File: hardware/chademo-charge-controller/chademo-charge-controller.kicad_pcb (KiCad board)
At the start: 2 copper layers, 136 x 120 mm, 26 parts, among them IC1 TPS62160DGKR, IC2 MCP2515-I_ST, IC3 SN65HVD230, IC4 MCP2515-I_ST, IC5 SN65HVD230, IC6 NCV8402ASTT1G, J1 M22-2510346, U1 Pico, U2 PC817, U3 PC817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

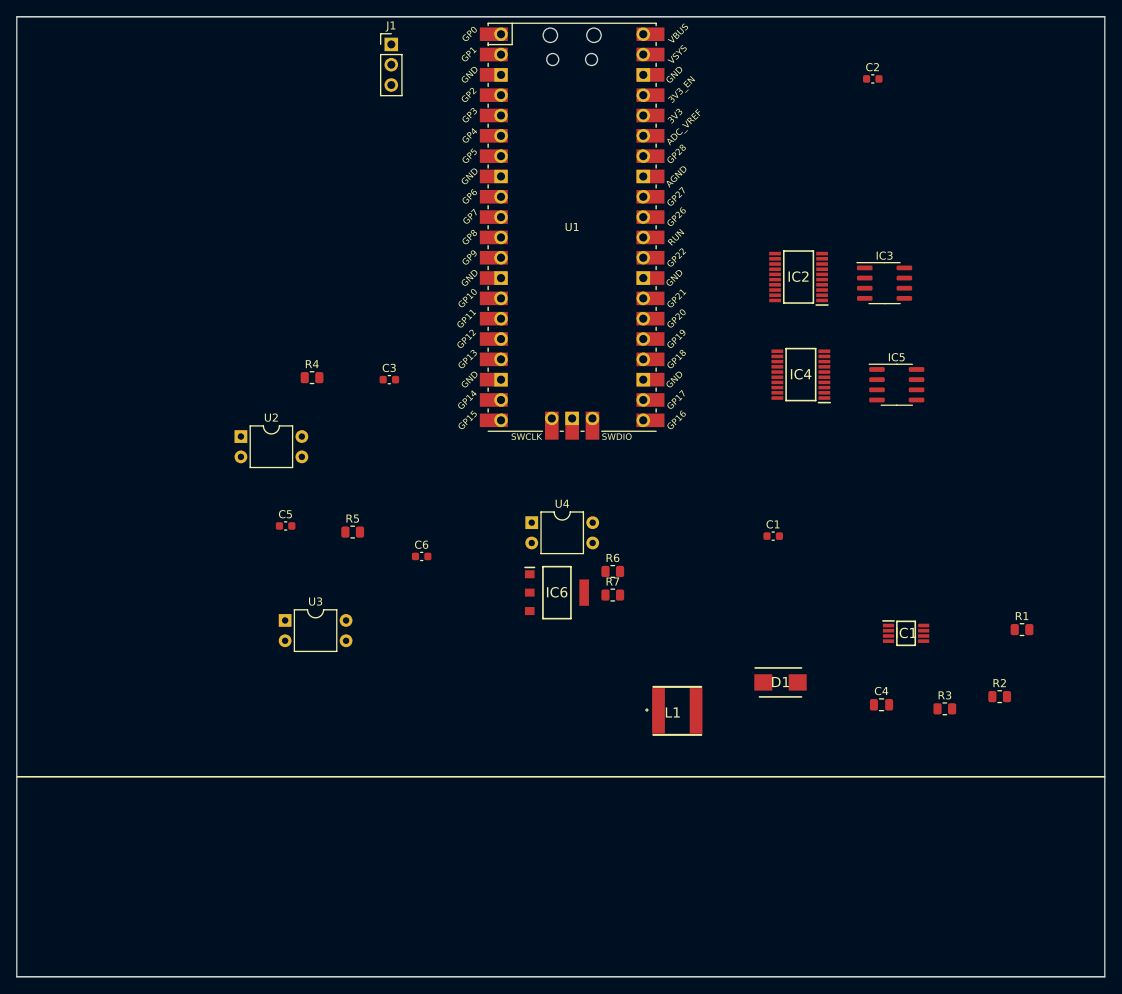
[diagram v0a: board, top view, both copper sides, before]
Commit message: pcb layout, 56pin socket
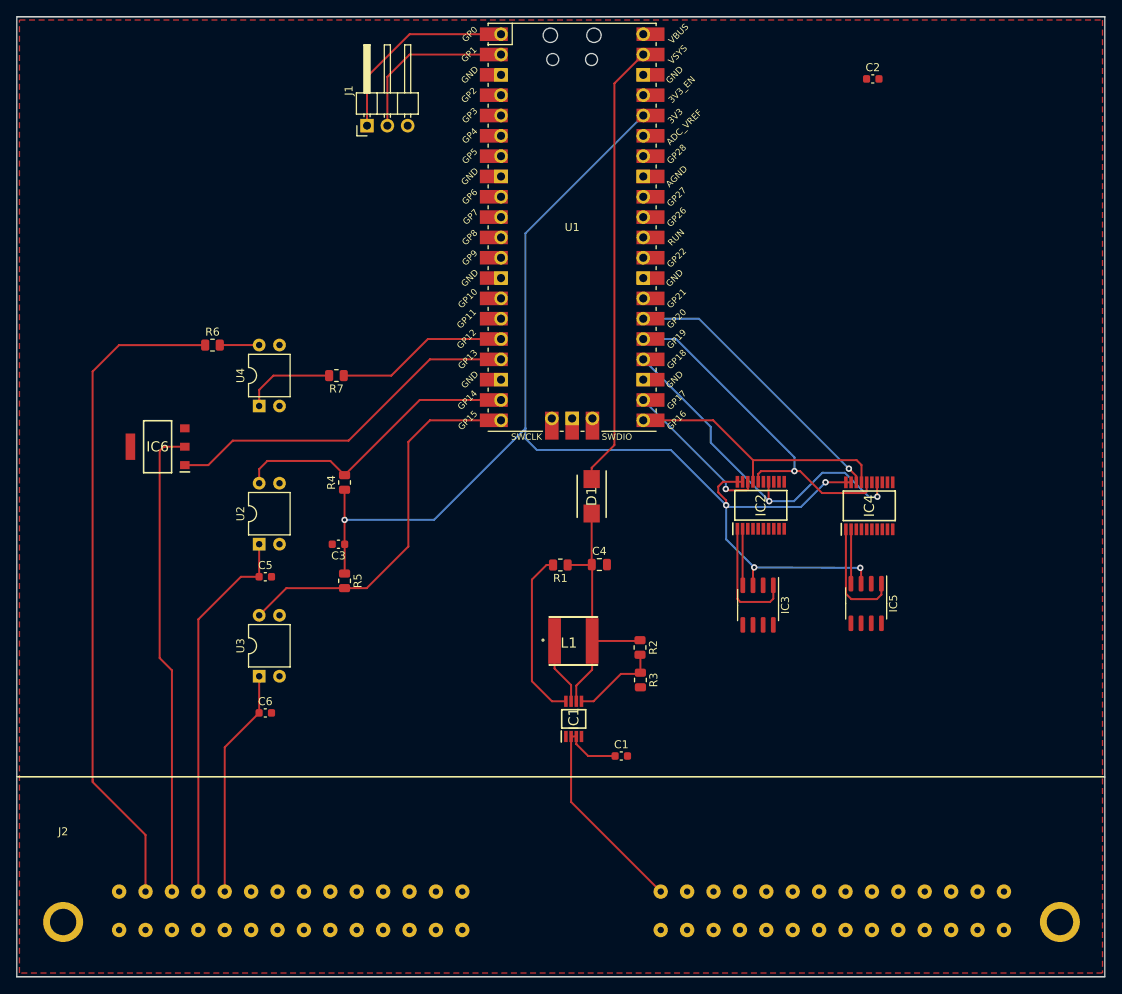
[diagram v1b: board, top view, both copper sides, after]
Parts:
- added J2: Conn_2Rows-57Pins, Connector:delphi56, F.Cu at (105.8, 127.3)
- J1: footprint Connector_PinHeader_2.54mm:PinHeader_1x03_P2.54mm_Vertical -> Connector_PinHeader_2.54mm:PinHeader_1x03_P2.54mm_Horizontal
- moved R1 58.3 mm to (167.9, 93.5), turned to 180 degrees
- moved R6 57.5 mm to (124.5, 66.0)
- moved IC6 53.1 mm to (117.6, 78.7), turned to 180 degrees
- moved R2 45.4 mm to (177.9, 103.8), turned to -90 degrees
- moved R7 44.1 mm to (140.0, 69.8), turned to 180 degrees
- moved IC3 43.2 mm to (192.7, 98.5), turned to -90 degrees
- moved IC1 42.9 mm to (169.6, 112.8), turned to 90 degrees
- moved C4 39.4 mm to (172.8, 93.5)
- moved R3 38.2 mm to (178.0, 107.9), turned to -90 degrees
- moved U4 37.1 mm to (130.3, 73.7), turned to 90 degrees
- moved C1 33.4 mm to (175.6, 117.4)
- moved D1 33.1 mm to (171.9, 84.9), turned to -90 degrees
- moved IC2 28.9 mm to (193.0, 86.1), turned to 90 degrees
- moved C6 27.6 mm to (131.1, 112.0)
- moved IC5 27.6 mm to (206.2, 98.3), turned to -90 degrees
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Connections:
- IC6 pad 1: CONTACTOR_ENABLE -> OUT_2_CONTACTOR_ENABLE
- R7 pad 1: CHARGE_ENABLE -> OUT_1_CHARGE_ENABLE
- U1 pad 16: CONTACTOR_ENABLE -> OUT_1_CHARGE_ENABLE
- U1 pad 17: CHARGE_ENABLE -> OUT_2_CONTACTOR_ENABLE
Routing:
- net 3V: track 0.00 -> 162.8 mm, vias 0 -> 5
- net CP3: track 0.00 -> 83.2 mm
- net OUT2: track 0.00 -> 59.1 mm
- net Net-(U1-VSYS): track 0.00 -> 55.7 mm
- net IN2: track 0.00 -> 48.0 mm
- net CP: track 0.00 -> 47.9 mm
- net OUT_2_CONTACTOR_ENABLE: track 0.00 -> 45.0 mm
- net SPI0_CLK: track 0.00 -> 44.8 mm, vias 0 -> 2
- net SPI0_MOSI: track 0.00 -> 43.8 mm, vias 0 -> 1
- net IN1: track 0.00 -> 37.0 mm
- net CHADEMO_CS: track 0.00 -> 35.6 mm, vias 0 -> 1
- net SPI0_MISO: track 0.00 -> 34.5 mm
- net 5V: track 0.00 -> 33.4 mm
- net 12V: track 0.00 -> 31.1 mm
- net CP2: track 0.00 -> 28.7 mm
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- added copper zone on F.Cu, net GND

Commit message: tweaking hw
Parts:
- added D2: LED, LED_SMD:LED_0805_2012Metric, F.Cu at (108.4, 31.8)
- added D3: LED, LED_SMD:LED_0805_2012Metric, F.Cu at (108.4, 36.8)
- added D4: LED, LED_SMD:LED_0805_2012Metric, F.Cu at (108.4, 41.9)
- added D5: LED, LED_SMD:LED_0805_2012Metric, F.Cu at (108.4, 47.0)
- added R10: 1k, Resistor_SMD:R_0805_2012Metric, F.Cu at (122.7, 102.6)
- added R11: 50, Resistor_SMD:R_0805_2012Metric, F.Cu at (127.6, 47.0)
- added R8: 50, Resistor_SMD:R_0805_2012Metric, F.Cu at (127.6, 36.8)
- added R9: 50, Resistor_SMD:R_0805_2012Metric, F.Cu at (127.6, 41.9)
- R5: value 1k -> 50
- moved R5 65.1 mm to (127.6, 31.8), turned to 180 degrees
- moved C2 51.7 mm to (200.4, 84.1), turned to -90 degrees
- moved C3 47.0 mm to (186.7, 84.1), turned to -90 degrees
- moved D1 30.0 mm to (169.2, 114.8)
- moved C6 22.2 mm to (109.5, 106.7), turned to 180 degrees
- moved C5 22.1 mm to (109.5, 90.4), turned to 180 degrees
- moved R7 21.3 mm to (121.7, 58.9)
- moved U4 19.8 mm to (113.8, 62.7)
- moved R4 18.6 mm to (122.7, 86.6), turned to 180 degrees
- moved R6 17.6 mm to (108.3, 58.9)
- moved U3 16.0 mm to (114.3, 106.7)
- moved U2 16.0 mm to (114.3, 90.4)
- moved IC1 8.03 mm to (169.6, 104.7)
- moved L1 8.03 mm to (169.6, 95.0)
- moved R1 8.03 mm to (168.0, 85.5)
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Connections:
- C1 pad 1: 12V -> Net-(IC1-EN)
- D1 pad 1: Net-(U1-VSYS) -> Net-(IC1-EN)
- D1 pad 2: 5V -> 12V
- IC1 pad 2: 12V -> Net-(IC1-EN)
- IC1 pad 3: 12V -> Net-(IC1-EN)
- J2 pad 21: unconnected-(J2-Pin_21-Pad21) -> MAIN_CAN_H
- J2 pad 23: unconnected-(J2-Pin_23-Pad23) -> CHADEMO_CAN_H
- J2 pad 28: unconnected-(J2-Pin_28-Pad28) -> GND
- J2 pad 43: unconnected-(J2-Pin_43-Pad43) -> GND
- J2 pad 49: unconnected-(J2-Pin_49-Pad49) -> MAIN_CAN_L
- J2 pad 51: unconnected-(J2-Pin_51-Pad51) -> CHADEMO_CAN_L
- R5 pad 2: IN2 -> Net-(D2-A)
- U1 pad 39: Net-(U1-VSYS) -> 5V
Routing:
- net 3V: track 162.8 -> 265.2 mm, vias 5 -> 6
- net IN2: track 48.0 -> 141.0 mm, vias 0 -> 1
- net IN1: track 37.0 -> 121.7 mm, vias 0 -> 1
- net 8MHz: track 0.00 -> 80.0 mm, vias 0 -> 3
- net OUT2: track 59.1 -> 118.8 mm, vias 0 -> 2
- net Net-(U1-VSYS): track 55.7 -> 0.00 mm
- net 5V: track 33.4 -> 85.4 mm
- net MAIN_CAN_L: track 0.00 -> 41.6 mm
- net CHADEMO_CAN_L: track 0.00 -> 39.2 mm
- net MAIN_CAN_H: track 0.00 -> 36.2 mm
- net CHADEMO_CAN_H: track 0.00 -> 33.6 mm
- net Net-(D4-K): track 4.93 -> 29.3 mm, vias 0 -> 1
- net OUT_1_CHARGE_ENABLE: track 21.6 -> 43.3 mm
- net Net-(D4-A): track 0.00 -> 17.3 mm
- net Net-(D3-A): track 0.00 -> 17.3 mm
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- added copper zone on B.Cu, net GND
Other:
- board text added: "IN1/CP"
- board text added: "IN2/CP2"
- board text added: "OUT1/CP3"
- board text added: "OUT2"

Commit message: lots of work on hardware
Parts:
- added C7: 10uF, Capacitor_SMD:C_0603_1608Metric, F.Cu at (132.7, 92.7)
- added D6: LED, LED_SMD:LED_0805_2012Metric, F.Cu at (118.9, 32.3)
- added D7: LED, LED_SMD:LED_0805_2012Metric, F.Cu at (119.0, 46.8)
- added D8: LED, LED_SMD:LED_0805_2012Metric, F.Cu at (119.1, 49.9)
- added G***: LOGO, LOGO, F.Cu at (164.3, 114.5)
- added G***: LOGO, Connector:chademo-logo-10x10, F.Cu at (193.0, 49.8)
- added H1: MountingHole_Pad, MountingHole:MountingHole_3.2mm_M3_DIN965_Pad, F.Cu at (105.8, 39.1)
- added H2: MountingHole_Pad, MountingHole:MountingHole_3.2mm_M3_DIN965_Pad, F.Cu at (229.9, 39.1)
- added J3: Conn_01x02_Pin, Connector_PinHeader_2.54mm:PinHeader_1x02_P2.54mm_Vertical, F.Cu at (200.0, 115.6)
- added J7: Conn_01x02_Pin, Connector_PinHeader_2.54mm:PinHeader_1x02_P2.54mm_Vertical, F.Cu at (205.5, 39.1)
- added J8: Conn_01x02_Pin, Connector_PinHeader_2.54mm:PinHeader_1x02_P2.54mm_Vertical, F.Cu at (218.8, 115.6)
- added JP1: SolderJumper_2_Open, Jumper:SolderJumper-2_P1.3mm_Open_Pad1.0x1.5mm, F.Cu at (197.8, 110.6)
- added JP2: SolderJumper_2_Open, Jumper:SolderJumper-2_P1.3mm_Open_Pad1.0x1.5mm, F.Cu at (216.5, 111.0)
- added R12: 120, Resistor_SMD:R_0805_2012Metric, F.Cu at (204.2, 110.6)
- added R13: 120, Resistor_SMD:R_0805_2012Metric, F.Cu at (223.3, 111.0)
- added R14: 1k, Resistor_SMD:R_0805_2012Metric, F.Cu at (146.2, 113.3)
- added R15: 50, Resistor_SMD:R_0805_2012Metric, F.Cu at (150.9, 32.3)
- added R16: 1k, Resistor_SMD:R_0805_2012Metric, F.Cu at (132.8, 112.7)
- added R17: 560, Resistor_SMD:R_0805_2012Metric, F.Cu at (122.7, 114.6)
- added R18: 560, Resistor_SMD:R_0805_2012Metric, F.Cu at (108.7, 100.3)
- added R19: 560, Resistor_SMD:R_0805_2012Metric, F.Cu at (132.5, 96.2)
- added R20: 50, Resistor_SMD:R_0805_2012Metric, F.Cu at (150.8, 46.8)
- added R21: 1k, Resistor_SMD:R_0805_2012Metric, F.Cu at (147.1, 96.3)
- added R22: 100, Resistor_SMD:R_0805_2012Metric, F.Cu at (145.9, 67.1)
- added R23: 50, Resistor_SMD:R_0805_2012Metric, F.Cu at (150.7, 49.9)
- added U5: PC817, Package_DIP:DIP-4_W7.62mm, F.Cu at (137.9, 116.0)
- added U6: PC817, Package_DIP:DIP-4_W7.62mm, F.Cu at (137.9, 100.1)
- added U7: PC817, Package_DIP:DIP-4_W7.62mm, F.Cu at (137.9, 70.9)
- moved C4 63.2 mm to (216.3, 39.5)
- moved L1 63.2 mm to (213.0, 49.0)
- moved R1 63.2 mm to (211.4, 39.5)
- moved R2 63.2 mm to (221.4, 49.8)
- moved IC1 60.8 mm to (213.1, 62.2)
- moved R3 60.6 mm to (221.4, 61.1)
- moved C1 53.5 mm to (207.5, 66.5), turned to 180 degrees
- moved J1 37.2 mm to (180.3, 31.8), turned to 0 degrees
- moved R5 23.5 mm to (150.8, 35.4)
- moved R11 23.4 mm to (150.8, 43.9)
- moved R8 23.3 mm to (150.8, 38.3)
- moved R9 23.3 mm to (150.8, 41.1)
- moved D1 18.8 mm to (188.0, 113.5)
- moved U1 16.2 mm to (169.3, 67.5)
- moved IC5 14.9 mm to (220.0, 103.9)
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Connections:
- C1 pad 1: Net-(IC1-EN) -> 12V
- C5 pad 1: CP -> Net-(C5-Pad1)
- C6 pad 1: CP2 -> Net-(C6-Pad1)
- C6 pad 2: GND -> CP2
- D1 pad 1: Net-(IC1-EN) -> 12V
- D1 pad 2: 12V -> 12V_IN
- D5 pad 1: OUT2 -> CONTACTOR_NEG
- IC1 pad 2: Net-(IC1-EN) -> 12V
- IC1 pad 3: Net-(IC1-EN) -> 12V
- IC6 pad 2: OUT2 -> CONTACTOR_NEG
- IC6 pad 3: GND -> CP2
- J2 pad 12: unconnected-(J2-Pin_12-Pad12) -> CHARGE_ENABLE
- J2 pad 15: 12V -> 12V_IN
- J2 pad 20: unconnected-(J2-Pin_20-Pad20) -> MAIN_CAN_L
- J2 pad 22: unconnected-(J2-Pin_22-Pad22) -> CHADEMO_CAN_L
- J2 pad 28: GND -> unconnected-(J2-Pin_28-Pad28)
- J2 pad 32: unconnected-(J2-Pin_32-Pad32) -> CONCTACTOR_POS
- J2 pad 33: unconnected-(J2-Pin_33-Pad33) -> 12V
- J2 pad 36: unconnected-(J2-Pin_36-Pad36) -> PROX
- J2 pad 4: CP -> CONCTACTOR_POS
- J2 pad 42: unconnected-(J2-Pin_42-Pad42) -> GND
- J2 pad 49: MAIN_CAN_L -> unconnected-(J2-Pin_49-Pad49)
- J2 pad 51: CHADEMO_CAN_L -> unconnected-(J2-Pin_51-Pad51)
- J2 pad 56: unconnected-(J2-Pin_56-Pad56) -> GND
- J2 pad 7: unconnected-(J2-Pin_7-Pad7) -> CHARGE_INHIBIT
- J2 pad 8: unconnected-(J2-Pin_8-Pad8) -> MANUAL_WAKE_SWITCH_A
- J2 pad 9: unconnected-(J2-Pin_9-Pad9) -> 12V
- U1 pad 12: unconnected-(U1-GPIO9-Pad12) -> CHARGE_ENABLE_MCU
- U1 pad 14: unconnected-(U1-GPIO10-Pad14) -> CHARGE_INHIBIT_MCU
- U1 pad 15: unconnected-(U1-GPIO11-Pad15) -> MANUAL_WAKE_SWITCH_A
- U1 pad 29: WAKE -> unconnected-(U1-GPIO22-Pad29)
- U2 pad 1: CP -> Net-(C5-Pad1)
- U3 pad 1: CP2 -> Net-(C6-Pad1)
- U3 pad 2: GND -> CP2
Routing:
- net 12V: track 22.1 -> 301.6 mm
- net MANUAL_WAKE_SWITCH_A: track 0.00 -> 162.6 mm, vias 0 -> 3
- net OUT2: track 118.8 -> 0.00 mm, vias 2 -> 0
- net CHARGE_INHIBIT_MCU: track 0.00 -> 103.9 mm, vias 0 -> 2
- net CHARGE_ENABLE: track 0.00 -> 88.8 mm
- net CP: track 60.9 -> 0.00 mm
- net CONTACTOR_NEG: track 0.00 -> 59.5 mm, vias 0 -> 2
- net 3V: track 265.2 -> 318.8 mm, vias 6 -> 7
- net CP2: track 36.6 -> 89.6 mm, vias 0 -> 2
- net CONCTACTOR_POS: track 0.00 -> 46.7 mm
- net CHARGE_INHIBIT: track 0.00 -> 42.6 mm
- net PROX: track 0.00 -> 30.4 mm
- net Net-(D6-A): track 0.00 -> 30.1 mm
- net Net-(D7-A): track 0.00 -> 29.9 mm
- net Net-(D8-A): track 0.00 -> 29.8 mm
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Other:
- board size 136 x 120 mm -> 134 x 120 mm
- board text added: "12V"
- board text added: "3V"
- board text added: "5V"
- board text added: "CHARGE ENABLE"
- board text added: "CHARGE ENABLE [OUT]"
- board text added: "CHARGE INHIBIT"
- board text added: "CHARGE INHIBIT [IN]"
- board text added: "CHAdeMO CAN"
- board text added: "ELECTRIC MUSTANG CHAdeMO Charge Controller v1.0 © 2023"
- board text added: "GND"
- board text added: "HI"
- board text added: "LO"
- board text added: "MAIN CAN"
- board text added: "PICO UART"
- board text added: "POWER SUPPLY"
- board text added: "PROXIMITY"
- board text added: "RX"
- board text added: "SIGNAL STATUS"
- board text added: "TX"
- board text added: "https://github.com/chrskly/chademo-charge-controller https://chrskly.com"

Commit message: I dunno ... lots
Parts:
- added REF**: OSHW-Logo_11.4x12mm_SilkScreen, Symbol:OSHW-Logo_11.4x12mm_SilkScreen, F.Cu at (193.0, 63.0)
- R10, R16, R21, R4: value 1k -> 1k6
- R11, R15, R20, R23, R5, R8, R9: value 50 -> 10
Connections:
- D8 pad 1: 12V -> GND
- J2 pad 3: OUT2 -> CONTACTOR_NEG
- R23 pad 1: 3V -> CHARGE_ENABLE_MCU
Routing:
- net CONTACTOR_NEG: track 59.5 -> 123.3 mm
- net 12V: track 301.6 -> 270.8 mm
- net CHARGE_ENABLE_MCU: track 15.3 -> 32.5 mm
- net CHARGE_INHIBIT_MCU: track 103.9 -> 99.2 mm
- net 3V: track 318.8 -> 315.8 mm
- net CONCTACTOR_POS: track 46.7 -> 45.0 mm
- net CP2: track 89.6 -> 91.1 mm
